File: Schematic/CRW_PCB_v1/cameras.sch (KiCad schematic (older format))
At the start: 9 parts

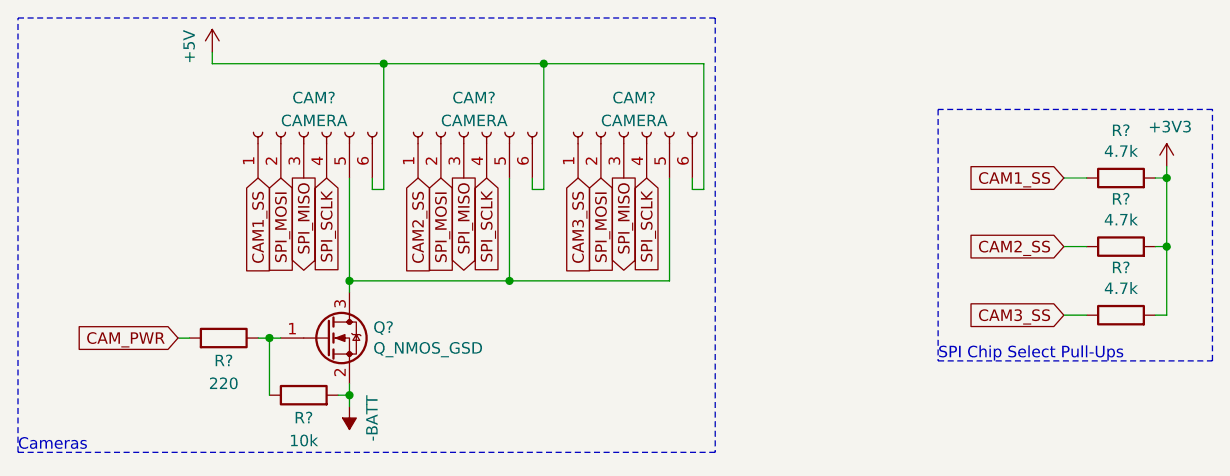
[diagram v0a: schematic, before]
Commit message: Added Hotwire Connection
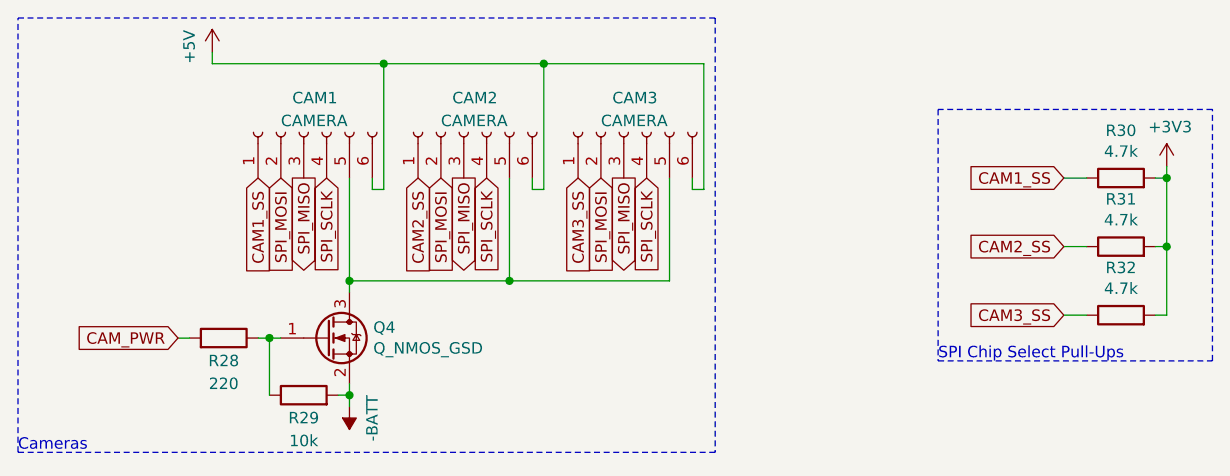
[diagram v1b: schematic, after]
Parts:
- gave numbers to parts that had none: 9
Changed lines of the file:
@@
 P 3675 4150
 AR Path="/5FF125E0" Ref="R?"  Part="1"
-AR Path="/5FEC70F1/5FF125E0" Ref="R?"  Part="1"
-F 0 "R?" V 3575 4150 50  0000 C CNN
+AR Path="/5FEC70F1/5FF125E0" Ref="R28"  Part="1"
+F 0 "R28" V 3575 4150 50  0000 C CNN
 F 1 "220" V 3475 4150 50  0000 C CNN
 F 2 "Resistor_SMD:R_0603_1608Metric_Pad0.98x0.95mm_HandSolder" V 3605 4150 50  0001 C CNN
@@
 P 4025 4400
 AR Path="/5FF12608" Ref="R?"  Part="1"
-AR Path="/5FEC70F1/5FF12608" Ref="R?"  Part="1"
-F 0 "R?" V 3925 4400 50  0000 C CNN
+AR Path="/5FEC70F1/5FF12608" Ref="R29"  Part="1"
+F 0 "R29" V 3925 4400 50  0000 C CNN
 F 1 "10k" V 3825 4400 50  0000 C CNN
 F 2 "Resistor_SMD:R_0402_1005Metric_Pad0.72x0.64mm_HandSolder" V 3955 4400 50  0001 C CNN
@@
 P 4125 4150
 AR Path="/5FF12610" Ref="Q?"  Part="1"
-AR Path="/5FEC70F1/5FF12610" Ref="Q?"  Part="1"
-F 0 "Q?" H 4329 4196 50  0000 L CNN
+AR Path="/5FEC70F1/5FF12610" Ref="Q4"  Part="1"
+F 0 "Q4" H 4329 4196 50  0000 L CNN
 F 1 "Q_NMOS_GSD" H 4329 4105 50  0000 L CNN
 F 2 "Package_TO_SOT_SMD:SC-59_Handsoldering" H 4325 4250 50  0001 C CNN
@@
 P 4225 4450
 AR Path="/5FF12623" Ref="#PWR?"  Part="1"
-AR Path="/5FEC70F1/5FF12623" Ref="#PWR?"  Part="1"
-F 0 "#PWR?" H 4225 4300 50  0001 C CNN
+AR Path="/5FEC70F1/5FF12623" Ref="#PWR050"  Part="1"
+F 0 "#PWR050" H 4225 4300 50  0001 C CNN
 F 1 "-BATT" V 4125 4400 50  0000 L CNN
 F 2 "" H 4225 4450 50  0001 C CNN
@@
 P 3625 2900
 AR Path="/5FF12629" Ref="#PWR?"  Part="1"
-AR Path="/5FEC70F1/5FF12629" Ref="#PWR?"  Part="1"
-F 0 "#PWR?" H 3625 2750 50  0001 C CNN
+AR Path="/5FEC70F1/5FF12629" Ref="#PWR047"  Part="1"
+F 0 "#PWR047" H 3625 2750 50  0001 C CNN
 F 1 "+5V" V 3525 2850 50  0000 L CNN
 F 2 "" H 3625 2900 50  0001 C CNN
@@
 P 5425 3250
 AR Path="/5FF1262F" Ref="CAM?"  Part="1"
-AR Path="/5FEC70F1/5FF1262F" Ref="CAM?"  Part="1"
-F 0 "CAM?" V 5575 3300 50  0000 R CNN
+AR Path="/5FEC70F1/5FF1262F" Ref="CAM3"  Part="1"
+F 0 "CAM3" V 5575 3300 50  0000 R CNN
 F 1 "CAMERA" V 5475 3350 50  0000 R CNN
 F 2 "Connector_JST:JST_SH_BM06B-SRSS-TB_1x06-1MP_P1.00mm_Vertical" H 5425 3250 50  0001 C CNN
@@
 P 4725 3250
 AR Path="/5FF12635" Ref="CAM?"  Part="1"
-AR Path="/5FEC70F1/5FF12635" Ref="CAM?"  Part="1"
-F 0 "CAM?" V 4875 3300 50  0000 R CNN
+AR Path="/5FEC70F1/5FF12635" Ref="CAM2"  Part="1"
+F 0 "CAM2" V 4875 3300 50  0000 R CNN
 F 1 "CAMERA" V 4775 3350 50  0000 R CNN
 F 2 "Connector_JST:JST_SH_BM06B-SRSS-TB_1x06-1MP_P1.00mm_Vertical" H 4725 3250 50  0001 C CNN
@@
 P 4025 3250
 AR Path="/5FF1263B" Ref="CAM?"  Part="1"
-AR Path="/5FEC70F1/5FF1263B" Ref="CAM?"  Part="1"
-F 0 "CAM?" V 4175 3300 50  0000 R CNN
+AR Path="/5FEC70F1/5FF1263B" Ref="CAM1"  Part="1"
+F 0 "CAM1" V 4175 3300 50  0000 R CNN
 F 1 "CAMERA" V 4075 3350 50  0000 R CNN
 F 2 "Connector_JST:JST_SH_BM06B-SRSS-TB_1x06-1MP_P1.00mm_Vertical" H 4025 3250 50  0001 C CNN
@@
 P 7800 3400
 AR Path="/5FF50E86" Ref="#PWR?"  Part="1"
-AR Path="/5FEC70F1/5FF50E86" Ref="#PWR?"  Part="1"
-F 0 "#PWR?" H 7800 3250 50  0001 C CNN
+AR Path="/5FEC70F1/5FF50E86" Ref="#PWR051"  Part="1"
+F 0 "#PWR051" H 7800 3250 50  0001 C CNN
 F 1 "+3V3" H 7815 3573 50  0000 C CNN
 F 2 "" H 7800 3400 50  0001 C CNN
@@
 P 7600 3450
 AR Path="/5FF50E94" Ref="R?"  Part="1"
-AR Path="/5FEC70F1/5FF50E94" Ref="R?"  Part="1"
-F 0 "R?" V 7807 3450 50  0000 C CNN
+AR Path="/5FEC70F1/5FF50E94" Ref="R30"  Part="1"
+F 0 "R30" V 7807 3450 50  0000 C CNN
 F 1 "4.7k" V 7716 3450 50  0000 C CNN
 F 2 "Resistor_SMD:R_0402_1005Metric_Pad0.72x0.64mm_HandSolder" V 7530 3450 50  0001 C CNN
@@
 P 7600 3750
 AR Path="/5FF50E9A" Ref="R?"  Part="1"
-AR Path="/5FEC70F1/5FF50E9A" Ref="R?"  Part="1"
-F 0 "R?" V 7807 3750 50  0000 C CNN
+AR Path="/5FEC70F1/5FF50E9A" Ref="R31"  Part="1"
+F 0 "R31" V 7807 3750 50  0000 C CNN
 F 1 "4.7k" V 7716 3750 50  0000 C CNN
 F 2 "Resistor_SMD:R_0402_1005Metric_Pad0.72x0.64mm_HandSolder" V 7530 3750 50  0001 C CNN
@@
 P 7600 4050
 AR Path="/5FF50EA0" Ref="R?"  Part="1"
-AR Path="/5FEC70F1/5FF50EA0" Ref="R?"  Part="1"
-F 0 "R?" V 7807 4050 50  0000 C CNN
+AR Path="/5FEC70F1/5FF50EA0" Ref="R32"  Part="1"
+F 0 "R32" V 7807 4050 50  0000 C CNN
 F 1 "4.7k" V 7716 4050 50  0000 C CNN
 F 2 "Resistor_SMD:R_0402_1005Metric_Pad0.72x0.64mm_HandSolder" V 7530 4050 50  0001 C CNN
